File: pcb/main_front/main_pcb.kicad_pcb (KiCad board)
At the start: 2 copper layers, 304.8 x 160.2 mm, 290 parts, among them J1 AVR-ISP-6, J2 USB_C_Receptacle_USB2.0, J3 Conn_01x16_Male, Q1 Q_NMOS_DGS, SW1 RESET, SW2 BOOT, SW3 BL_STEP, U1 ATmega32-16PU, Y1 Crystal

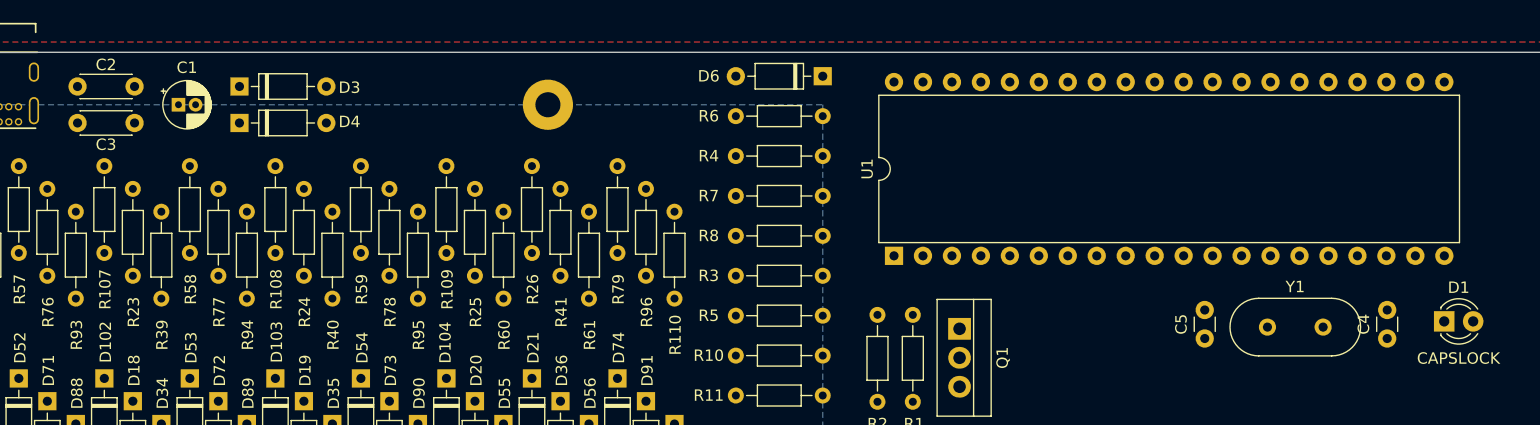
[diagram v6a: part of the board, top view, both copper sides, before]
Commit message: moved capacitors
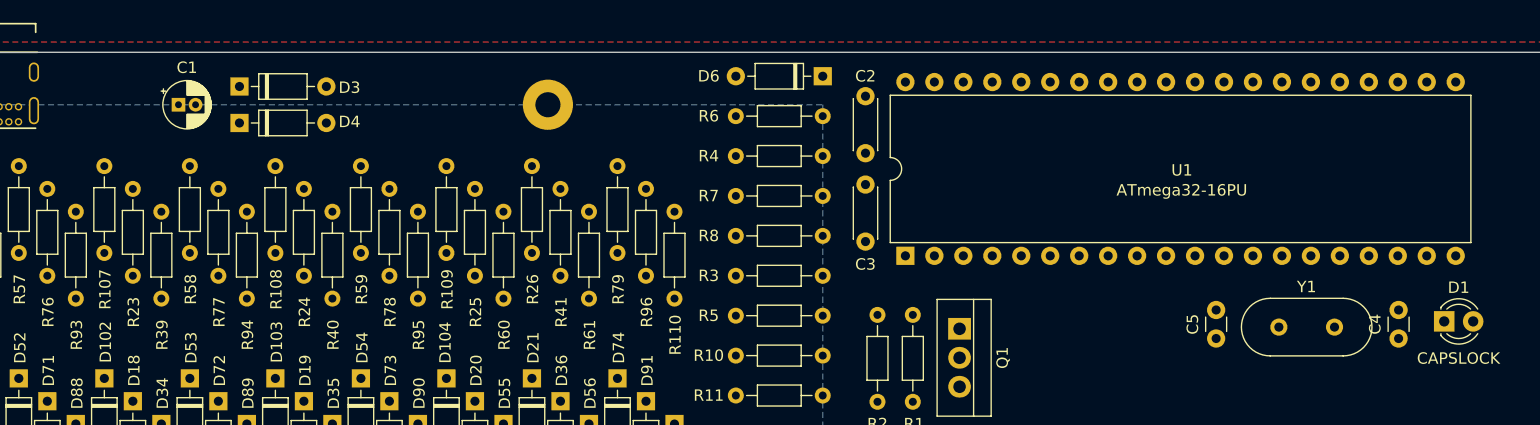
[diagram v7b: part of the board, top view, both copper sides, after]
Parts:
- moved C2 69.3 mm to (372.6, 143.1), turned to 90 degrees
- moved C3 69.3 mm to (372.6, 145.8), turned to 270 degrees
- moved C4 1.00 mm to (419.4, 159.3)
- moved C5 1.00 mm to (403.4, 159.3)
- moved U1 1.00 mm to (376.1, 152.1)
- moved Y1 1.00 mm to (408.9, 158.3)
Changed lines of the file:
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@@
   )
   (module Crystal:Crystal_HC49-4H_Vertical (layer F.Cu)
-    (at 407.9 158.3)
+    (at 408.9 158.3)
     (descr "Crystal THT HC-49-4H http://5hertz.com/pdfs/04404_D.pdf")
     (tags "THT crystalHC-49-4H")
@@
   )
   (module Package_DIP:DIP-40_W15.24mm (layer F.Cu)
-    (at 375.15 152.05 90)
+    (at 376.15 152.05 90)
     (descr "40-lead though-hole mounted DIP package, row spacing 15.24 mm (600 mils)")
     (tags "THT DIP DIL PDIP 2.54mm 15.24mm 600mil")
-    (fp_text reference U1 (at 7.62 -2.33 90) (layer F.SilkS)
+    (fp_text reference U1 (at 7.5 24.25 180) (layer F.SilkS)
       (effects (font (size 1 1) (thickness 0.15)))
     )
-    (fp_text value ATmega32-16PU (at 7.62 50.59 90) (layer F.Fab)
+    (fp_text value ATmega32-16PU (at 5.75 24.25 180) (layer F.SilkS)
       (effects (font (size 1 1) (thickness 0.15)))
     )
@@
   )
   (module Capacitor_THT:C_Disc_D3.0mm_W1.6mm_P2.50mm (layer F.Cu)
-    (at 402.4 159.3 90)
+    (at 403.4 159.3 90)
     (descr "C, Disc series, Radial, pin pitch=2.50mm, , diameter*width=3.0*1.6mm^2, Capacitor, http://www.vishay.com/docs/45233/krseries.pdf")
     (tags "C Disc series Radial pin pitch 2.50mm  diameter 3.0mm width 1.6mm Capacitor")
@@
   )
   (module Capacitor_THT:C_Disc_D3.0mm_W1.6mm_P2.50mm (layer F.Cu)
-    (at 418.4 159.3 90)
+    (at 419.4 159.3 90)
     (descr "C, Disc series, Radial, pin pitch=2.50mm, , diameter*width=3.0*1.6mm^2, Capacitor, http://www.vishay.com/docs/45233/krseries.pdf")
     (tags "C Disc series Radial pin pitch 2.50mm  diameter 3.0mm width 1.6mm Capacitor")
@@
   )
   (module Capacitor_THT:C_Disc_D4.3mm_W1.9mm_P5.00mm (layer F.Cu)
-    (at 303.55 140.4)
+    (at 372.65 145.8 270)
     (descr "C, Disc series, Radial, pin pitch=5.00mm, , diameter*width=4.3*1.9mm^2, Capacitor, http://www.vishay.com/docs/45233/krseries.pdf")
     (tags "C Disc series Radial pin pitch 5.00mm  diameter 4.3mm width 1.9mm Capacitor")
-    (fp_text reference C3 (at 2.5 1.9) (layer F.SilkS)
+    (fp_text reference C3 (at 7 0 180) (layer F.SilkS)
       (effects (font (size 1 1) (thickness 0.15)))
     )
-    (fp_text value 0.1u (at 2.5 2.2) (layer F.Fab)
+    (fp_text value 0.1u (at 2.5 2.2 90) (layer F.Fab)
       (effects (font (size 1 1) (thickness 0.15)))
     )
@@
     (fp_line (start 6.05 1.2) (end 6.05 -1.2) (layer F.CrtYd) (width 0.05))
     (fp_line (start 6.05 -1.2) (end -1.05 -1.2) (layer F.CrtYd) (width 0.05))
-    (fp_text user %R (at 2.5 0) (layer F.Fab)
+    (fp_text user %R (at 2.5 0 90) (layer F.Fab)
       (effects (font (size 0.86 0.86) (thickness 0.129)))
     )
-    (pad 2 thru_hole circle (at 5 0) (size 1.6 1.6) (drill 0.8) (layers *.Cu *.Mask)
+    (pad 2 thru_hole circle (at 5 0 270) (size 1.6 1.6) (drill 0.8) (layers *.Cu *.Mask)
       (net 1 GND))
-    (pad 1 thru_hole circle (at 0 0) (size 1.6 1.6) (drill 0.8) (layers *.Cu *.Mask)
+    (pad 1 thru_hole circle (at 0 0 270) (size 1.6 1.6) (drill 0.8) (layers *.Cu *.Mask)
       (net 2 +5V))
     (model ${KISYS3DMOD}/Capacitor_THT.3dshapes/C_Disc_D4.3mm_W1.9mm_P5.00mm.wrl
@@
   )
   (module Capacitor_THT:C_Disc_D4.3mm_W1.9mm_P5.00mm (layer F.Cu)
-    (at 303.55 137.2)
+    (at 372.65 143.05 90)
     (descr "C, Disc series, Radial, pin pitch=5.00mm, , diameter*width=4.3*1.9mm^2, Capacitor, http://www.vishay.com/docs/45233/krseries.pdf")
     (tags "C Disc series Radial pin pitch 5.00mm  diameter 4.3mm width 1.9mm Capacitor")
-    (fp_text reference C2 (at 2.5 -1.9) (layer F.SilkS)
+    (fp_text reference C2 (at 6.75 0 180) (layer F.SilkS)
       (effects (font (size 1 1) (thickness 0.15)))
     )
-    (fp_text value 0.1u (at 2.5 2.2) (layer F.Fab)
+    (fp_text value 0.1u (at 2.5 2.2 90) (layer F.Fab)
       (effects (font (size 1 1) (thickness 0.15)))
     )
@@
     (fp_line (start 6.05 1.2) (end 6.05 -1.2) (layer F.CrtYd) (width 0.05))
     (fp_line (start 6.05 -1.2) (end -1.05 -1.2) (layer F.CrtYd) (width 0.05))
-    (fp_text user %R (at 2.5 0) (layer F.Fab)
+    (fp_text user %R (at 2.5 0 90) (layer F.Fab)
       (effects (font (size 0.86 0.86) (thickness 0.129)))
     )
-    (pad 2 thru_hole circle (at 5 0) (size 1.6 1.6) (drill 0.8) (layers *.Cu *.Mask)
+    (pad 2 thru_hole circle (at 5 0 90) (size 1.6 1.6) (drill 0.8) (layers *.Cu *.Mask)
       (net 1 GND))
-    (pad 1 thru_hole circle (at 0 0) (size 1.6 1.6) (drill 0.8) (layers *.Cu *.Mask)
+    (pad 1 thru_hole circle (at 0 0 90) (size 1.6 1.6) (drill 0.8) (layers *.Cu *.Mask)
       (net 2 +5V))
     (model ${KISYS3DMOD}/Capacitor_THT.3dshapes/C_Disc_D4.3mm_W1.9mm_P5.00mm.wrl

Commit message: moved holes
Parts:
- removed the REF** at (344.8, 138.8)
- removed the REF** at (247.0, 138.8)
- removed the REF** at (443.8, 138.8)
- added REF**: MountingHole_2.2mm_M2_Pad, MountingHole:MountingHole_2.2mm_M2_Pad, F.Cu at (300.1, 285.0)
- added REF**: MountingHole_2.2mm_M2_Pad, MountingHole:MountingHole_2.2mm_M2_Pad, F.Cu at (247.0, 138.2)
- added REF**: MountingHole_2.2mm_M2_Pad, MountingHole:MountingHole_2.2mm_M2_Pad, F.Cu at (443.8, 138.2)
- added REF**: MountingHole_2.2mm_M2_Pad, MountingHole:MountingHole_2.2mm_M2_Pad, F.Cu at (295.3, 199.2)
- added REF**: MountingHole_2.2mm_M2_Pad, MountingHole:MountingHole_2.2mm_M2_Pad, F.Cu at (162.0, 199.1)
- added REF**: MountingHole_2.2mm_M2_Pad, MountingHole:MountingHole_2.2mm_M2_Pad, F.Cu at (428.7, 199.2)
- added REF**: MountingHole_2.2mm_M2_Pad, MountingHole:MountingHole_2.2mm_M2_Pad, F.Cu at (428.7, 275.3)
- added REF**: MountingHole_2.2mm_M2_Pad, MountingHole:MountingHole_2.2mm_M2_Pad, F.Cu at (166.7, 284.9)
- added REF**: MountingHole_2.2mm_M2_Pad, MountingHole:MountingHole_2.2mm_M2_Pad, F.Cu at (344.8, 138.2)
- moved REF** 0.60 mm to (147.0, 138.2)
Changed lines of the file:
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@@
     (tracks 0)
     (zones 0)
-    (modules 290)
+    (modules 296)
     (nets 222)
   )
@@
   )
   (module MountingHole:MountingHole_2.2mm_M2_Pad (layer F.Cu)
-    (at 344.8 176.204)
+    (at 300.1 285)
     (descr "Mounting Hole 2.2mm, M2")
     (tags "mounting hole 2.2mm m2")
@@
       (effects (font (size 1 1) (thickness 0.15)))
     )
-    (pad 1 thru_hole circle (at 0 -0.004) (size 4.4 4.4) (drill 2.2) (layers *.Cu *.Mask))
+    (pad 1 thru_hole circle (at 0 -0.008) (size 4.4 4.4) (drill 2.2) (layers *.Cu *.Mask))
+  )
+  (module MountingHole:MountingHole_2.2mm_M2_Pad (layer F.Cu)
+    (at 295.3 199.2)
+    (descr "Mounting Hole 2.2mm, M2")
+    (tags "mounting hole 2.2mm m2")
+    (attr virtual)
+    (fp_text reference REF** (at 0 -3.2) (layer F.SilkS) hide
+      (effects (font (size 1 1) (thickness 0.15)))
+    )
+    (fp_text value MountingHole_2.2mm_M2_Pad (at 0 3.2) (layer F.Fab)
+      (effects (font (size 1 1) (thickness 0.15)))
+    )
+    (fp_text user %R (at 0.3 0) (layer F.Fab)
+      (effects (font (size 1 1) (thickness 0.15)))
+    )
+    (fp_circle (center 0 0) (end 2.2 0) (layer Cmts.User) (width 0.15))
+    (fp_circle (center 0 0) (end 2.45 0) (layer F.CrtYd) (width 0.05))
+    (pad 1 thru_hole circle (at 0 -0.008) (size 4.4 4.4) (drill 2.2) (layers *.Cu *.Mask))
   )
   (module MountingHole:MountingHole_2.2mm_M2_Pad (layer F.Cu)
-    (at 344.8 138.808)
+    (at 162 199.108)
     (descr "Mounting Hole 2.2mm, M2")
     (tags "mounting hole 2.2mm m2")
@@
   )
   (module MountingHole:MountingHole_2.2mm_M2_Pad (layer F.Cu)
-    (at 247 176.204)
+    (at 428.7 199.2)
     (descr "Mounting Hole 2.2mm, M2")
     (tags "mounting hole 2.2mm m2")
@@
       (effects (font (size 1 1) (thickness 0.15)))
     )
-    (pad 1 thru_hole circle (at 0 -0.204) (size 4.4 4.4) (drill 2.2) (layers *.Cu *.Mask))
+    (pad 1 thru_hole circle (at 0 -0.008) (size 4.4 4.4) (drill 2.2) (layers *.Cu *.Mask))
+  )
+  (module MountingHole:MountingHole_2.2mm_M2_Pad (layer F.Cu)
+    (at 428.7 275.3)
+    (descr "Mounting Hole 2.2mm, M2")
+    (tags "mounting hole 2.2mm m2")
+    (attr virtual)
+    (fp_text reference REF** (at 0 -3.2) (layer F.SilkS) hide
+      (effects (font (size 1 1) (thickness 0.15)))
+    )
+    (fp_text value MountingHole_2.2mm_M2_Pad (at 0 3.2) (layer F.Fab)
+      (effects (font (size 1 1) (thickness 0.15)))
+    )
+    (fp_circle (center 0 0) (end 2.45 0) (layer F.CrtYd) (width 0.05))
+    (fp_circle (center 0 0) (end 2.2 0) (layer Cmts.User) (width 0.15))
+    (fp_text user %R (at 0.3 0) (layer F.Fab)
+      (effects (font (size 1 1) (thickness 0.15)))
+    )
+    (pad 1 thru_hole circle (at 0 -0.008) (size 4.4 4.4) (drill 2.2) (layers *.Cu *.Mask))
+  )
+  (module MountingHole:MountingHole_2.2mm_M2_Pad (layer F.Cu)
+    (at 166.7 284.9)
+    (descr "Mounting Hole 2.2mm, M2")
+    (tags "mounting hole 2.2mm m2")
+    (attr virtual)
+    (fp_text reference REF** (at 0 -3.2) (layer F.SilkS) hide
+      (effects (font (size 1 1) (thickness 0.15)))
+    )
+    (fp_text value MountingHole_2.2mm_M2_Pad (at 0 3.2) (layer F.Fab)
+      (effects (font (size 1 1) (thickness 0.15)))
+    )
+    (fp_circle (center 0 0) (end 2.45 0) (layer F.CrtYd) (width 0.05))
+    (fp_circle (center 0 0) (end 2.2 0) (layer Cmts.User) (width 0.15))
+    (fp_text user %R (at 0.3 0) (layer F.Fab)
+      (effects (font (size 1 1) (thickness 0.15)))
+    )
+    (pad 1 thru_hole circle (at 0 -0.008) (size 4.4 4.4) (drill 2.2) (layers *.Cu *.Mask))
+  )
+  (module MountingHole:MountingHole_2.2mm_M2_Pad (layer F.Cu)
+    (at 344.8 176.204)
+    (descr "Mounting Hole 2.2mm, M2")
+    (tags "mounting hole 2.2mm m2")
+    (attr virtual)
+    (fp_text reference REF** (at 0 -3.2) (layer F.SilkS) hide
+      (effects (font (size 1 1) (thickness 0.15)))
+    )
+    (fp_text value MountingHole_2.2mm_M2_Pad (at 0 3.2) (layer F.Fab)
+      (effects (font (size 1 1) (thickness 0.15)))
+    )
+    (fp_circle (center 0 0) (end 2.45 0) (layer F.CrtYd) (width 0.05))
+    (fp_circle (center 0 0) (end 2.2 0) (layer Cmts.User) (width 0.15))
+    (fp_text user %R (at 0.3 0) (layer F.Fab)
+      (effects (font (size 1 1) (thickness 0.15)))
+    )
+    (pad 1 thru_hole circle (at 0 -0.004) (size 4.4 4.4) (drill 2.2) (layers *.Cu *.Mask))
   )
   (module MountingHole:MountingHole_2.2mm_M2_Pad (layer F.Cu)
-    (at 247 138.808)
+    (at 344.8 138.208)
+    (descr "Mounting Hole 2.2mm, M2")
+    (tags "mounting hole 2.2mm m2")
+    (attr virtual)
+    (fp_text reference REF** (at 0 -3.2) (layer F.SilkS) hide
+      (effects (font (size 1 1) (thickness 0.15)))
+    )
+    (fp_text value MountingHole_2.2mm_M2_Pad (at 0 3.2) (layer F.Fab)
+      (effects (font (size 1 1) (thickness 0.15)))
+    )
+    (fp_text user %R (at 0.3 0) (layer F.Fab)
+      (effects (font (size 1 1) (thickness 0.15)))
+    )
+    (fp_circle (center 0 0) (end 2.2 0) (layer Cmts.User) (width 0.15))
+    (fp_circle (center 0 0) (end 2.45 0) (layer F.CrtYd) (width 0.05))
+    (pad 1 thru_hole circle (at 0 -0.008) (size 4.4 4.4) (drill 2.2) (layers *.Cu *.Mask))
+  )
+  (module MountingHole:MountingHole_2.2mm_M2_Pad (layer F.Cu)
+    (at 247 176.204)
     (descr "Mounting Hole 2.2mm, M2")
     (tags "mounting hole 2.2mm m2")
@@
       (effects (font (size 1 1) (thickness 0.15)))
     )
+    (pad 1 thru_hole circle (at 0 -0.204) (size 4.4 4.4) (drill 2.2) (layers *.Cu *.Mask))
+  )
+  (module MountingHole:MountingHole_2.2mm_M2_Pad (layer F.Cu)
+    (at 247 138.208)
+    (descr "Mounting Hole 2.2mm, M2")
+    (tags "mounting hole 2.2mm m2")
+    (attr virtual)
+    (fp_text reference REF** (at 0 -3.2) (layer F.SilkS) hide
+      (effects (font (size 1 1) (thickness 0.15)))
+    )
+    (fp_text value MountingHole_2.2mm_M2_Pad (at 0 3.2) (layer F.Fab)
+      (effects (font (size 1 1) (thickness 0.15)))
+    )
+    (fp_text user %R (at 0.3 0) (layer F.Fab)
+      (effects (font (size 1 1) (thickness 0.15)))
+    )
+    (fp_circle (center 0 0) (end 2.2 0) (layer Cmts.User) (width 0.15))
+    (fp_circle (center 0 0) (end 2.45 0) (layer F.CrtYd) (width 0.05))
     (pad 1 thru_hole circle (at 0 -0.008) (size 4.4 4.4) (drill 2.2) (layers *.Cu *.Mask))
   )
@@
   )
   (module MountingHole:MountingHole_2.2mm_M2_Pad (layer F.Cu)
-    (at 443.8 138.804)
+    (at 443.8 138.204)
     (descr "Mounting Hole 2.2mm, M2")
     (tags "mounting hole 2.2mm m2")
@@
       (effects (font (size 1 1) (thickness 0.15)))
     )
-    (fp_circle (center 0 0) (end 2.45 0) (layer F.CrtYd) (width 0.05))
-    (fp_circle (center 0 0) (end 2.2 0) (layer Cmts.User) (width 0.15))
     (fp_text user %R (at 0.3 0) (layer F.Fab)
       (effects (font (size 1 1) (thickness 0.15)))
     )
+    (fp_circle (center 0 0) (end 2.2 0) (layer Cmts.User) (width 0.15))
+    (fp_circle (center 0 0) (end 2.45 0) (layer F.CrtYd) (width 0.05))
     (pad 1 thru_hole circle (at 0 -0.004) (size 4.4 4.4) (drill 2.2) (layers *.Cu *.Mask))
   )
   (module MountingHole:MountingHole_2.2mm_M2_Pad (layer F.Cu)
-    (at 147 138.804)
+    (at 147 138.204)
     (descr "Mounting Hole 2.2mm, M2")
     (tags "mounting hole 2.2mm m2")
@@
       (effects (font (size 1 1) (thickness 0.15)))
     )
-    (fp_circle (center 0 0) (end 2.2 0) (layer Cmts.User) (width 0.15))
-    (fp_circle (center 0 0) (end 2.45 0) (layer F.CrtYd) (width 0.05))
     (fp_text user %R (at 0.3 0) (layer F.Fab)
       (effects (font (size 1 1) (thickness 0.15)))
     )
+    (fp_circle (center 0 0) (end 2.45 0) (layer F.CrtYd) (width 0.05))
+    (fp_circle (center 0 0) (end 2.2 0) (layer Cmts.User) (width 0.15))
     (pad 1 thru_hole circle (at 0 -0.004) (size 4.4 4.4) (drill 2.2) (layers *.Cu *.Mask))
   )
@@
   (gr_line (start 396.9 155.45) (end 396.9 166.45) (layer Dwgs.User) (width 0.15))
   (gr_line (start 443.8 176.2) (end 147 176.2) (layer Dwgs.User) (width 0.15))
-  (gr_line (start 443.8 138.8) (end 443.8 176.2) (layer Dwgs.User) (width 0.15))
-  (gr_line (start 147 138.8) (end 443.8 138.8) (layer Dwgs.User) (width 0.15))
-  (gr_line (start 147 176.2) (end 147 138.8) (layer Dwgs.User) (width 0.15))
+  (gr_line (start 443.8 138.2) (end 443.8 176.2) (layer Dwgs.User) (width 0.15))
+  (gr_line (start 147 138.2) (end 443.8 138.2) (layer Dwgs.User) (width 0.15))
+  (gr_line (start 147 176.2) (end 147 138.2) (layer Dwgs.User) (width 0.15))
   (dimension 304.78125 (width 0.12) (layer Dwgs.User)
     (gr_text "304.781 mm" (at 295.334375 308.47) (layer Dwgs.User)
@@
     (polygon
       (pts
-        (xy 368.9 176.3) (xy 146.9 176.3) (xy 146.9 138.8) (xy 368.9 138.8)
+        (xy 368.6 176.2) (xy 147 176.2) (xy 147 138.2) (xy 368.6 138.2)
       )
     )
